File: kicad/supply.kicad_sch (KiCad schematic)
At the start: 52 parts, among them J5 Screw_Terminal_01x02, J6 Screw_Terminal_01x02, U14 TMUX6123, U17 TMUX6123, U19 L7815, U23 L7915, U6 LM2937-5, U9 LM317_TO-252

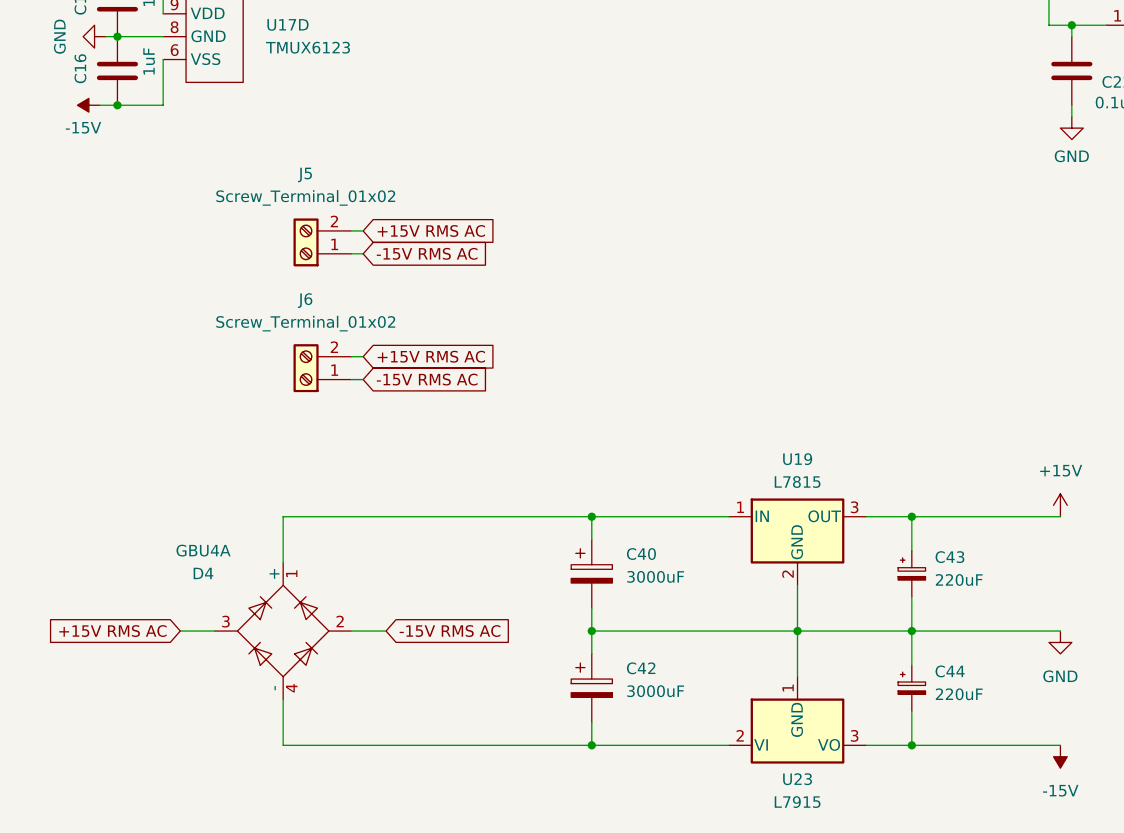
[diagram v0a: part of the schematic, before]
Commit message: Removed large cap and rectifier, added transistor resistors
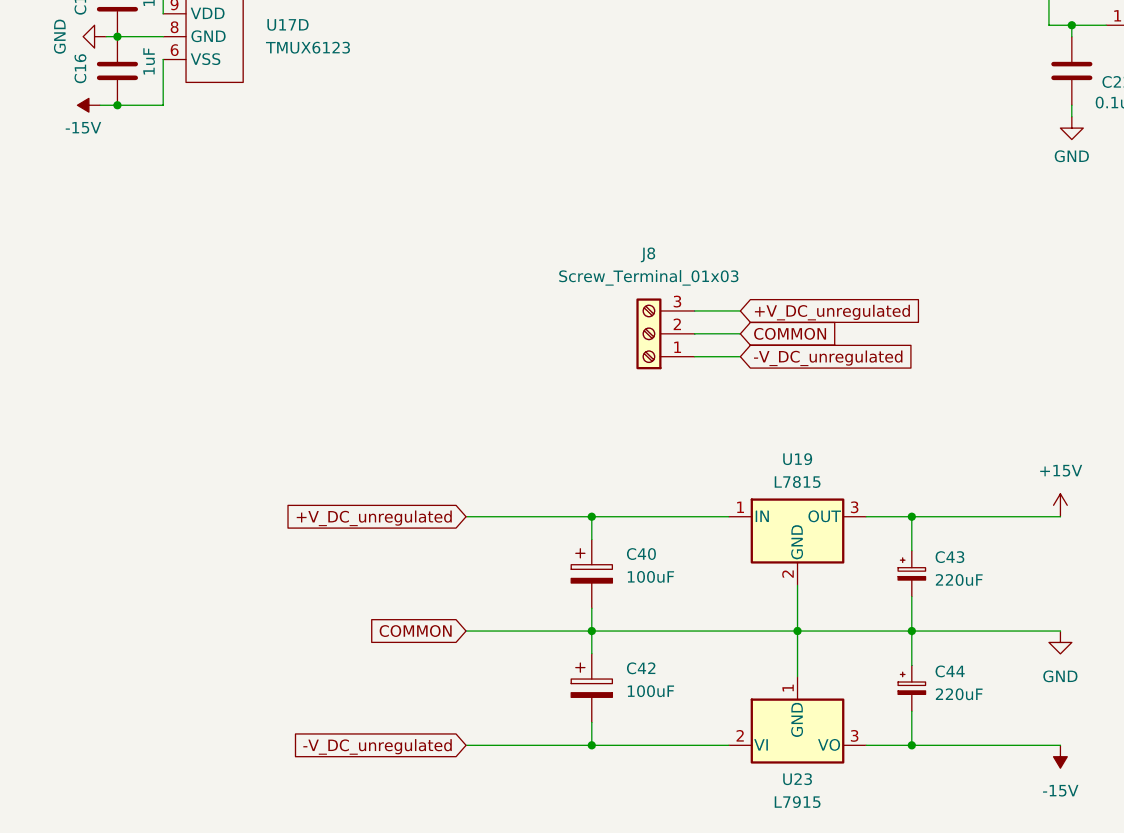
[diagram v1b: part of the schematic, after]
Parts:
- removed D4: GBU4A, Diode_THT:Diode_Bridge_Vishay_GBU, symbol Diode_Bridge:GBU4A
- removed J5, J6: Screw_Terminal_01x02, TerminalBlock_4Ucon:TerminalBlock_4Ucon_1x02_P3.50mm_Horizontal, symbol Connector:Screw_Terminal_01x02
- added J8: Screw_Terminal_01x03, TerminalBlock_4Ucon:TerminalBlock_4Ucon_1x03_P3.50mm_Horizontal, symbol Connector:Screw_Terminal_01x03
- C40, C42: value 3000uF -> 100uF; footprint Capacitor_SMD:CP_Elec_18x22 -> Capacitor_SMD:CP_Elec_8x6.5; DIGIKEY P122523CT-ND -> 1189-35PJV100M6.3X8TR-ND; PARTNO EEE-FK1V302SV -> 35PJV100M6.3X8
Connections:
- net GND: now also J8.2 (Pin_2)
- net +V_DC_unregulated: now reaches C40.1, U19.1 (IN)
- net +V_DC_unregulated: now also J8.3 (Pin_3)
- net -V_DC_unregulated: now reaches C42.2, U23.2 (VI)
- net -V_DC_unregulated: now also J8.1 (Pin_1)

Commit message: Final Schematic, Reworking PCB pt 1
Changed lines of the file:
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@@
 	(wire
 		(pts
-			(xy 72.39 168.91) (xy 86.36 168.91)
-		)
-		(stroke
-			(width 0)
-			(type default)
-		)
-	)
-	(wire
-		(pts
 			(xy 176.53 62.865) (xy 176.53 66.675)
 		)
@@
 	(wire
 		(pts
-			(xy 97.79 135.89) (xy 102.87 135.89)
-		)
-		(stroke
-			(width 0)
-			(type default)
-		)
-	)
-	(wire
-		(pts
 			(xy 160.655 52.07) (xy 176.53 52.07)
 		)
@@
 	(wire
 		(pts
+			(xy 130.81 138.43) (xy 130.81 135.89)
+		)
+		(stroke
+			(width 0)
+			(type default)
+		)
+	)
+	(wire
+		(pts
 			(xy 226.06 112.395) (xy 226.06 113.03)
 		)
@@
 	(wire
 		(pts
+			(xy 130.81 135.89) (xy 97.79 135.89)
+		)
+		(stroke
+			(width 0)
+			(type default)
+		)
+	)
+	(wire
+		(pts
 			(xy 78.74 49.53) (xy 78.74 52.07)
 		)
@@
 		)
 	)
-	(global_label "COMMON"
-		(shape input)
-		(at 72.39 168.91 180)
-		(fields_autoplaced yes)
-		(effects
-			(font
-				(size 1.27 1.27)
-			)
-			(justify right)
-		)
-		(property "Intersheetrefs" "${INTERSHEET_REFS}"
-			(at 61.2405 168.91 0)
-			(effects
-				(font
-					(size 1.27 1.27)
-				)
-				(justify right)
-				(hide yes)
-			)
-		)
-	)
 	(global_label "+V_DC_unregulated"
 		(shape input)
@@
 		)
 	)
-	(global_label "COMMON"
-		(shape input)
-		(at 102.87 135.89 0)
-		(fields_autoplaced yes)
-		(effects
-			(font
-				(size 1.27 1.27)
-			)
-			(justify left)
-		)
-		(property "Intersheetrefs" "${INTERSHEET_REFS}"
-			(at 114.0195 135.89 0)
-			(effects
-				(font
-					(size 1.27 1.27)
-				)
-				(justify left)
-				(hide yes)
-			)
-		)
-	)
 	(global_label "-V_DC_unregulated"
 		(shape input)
@@
 					(unit 1)
 				)
+			)
+		)
+	)
+	(symbol
+		(lib_id "power:GND")
+		(at 130.81 138.43 0)
+		(unit 1)
+		(exclude_from_sim no)
+		(in_bom yes)
+		(on_board yes)
+		(dnp no)
+		(fields_autoplaced yes)
+		(property "Reference" "#PWR081"
+			(at 130.81 144.78 0)
+			(effects
+				(font
+					(size 1.27 1.27)
+				)
+				(hide yes)
+			)
+		)
+		(property "Value" "GND"
+			(at 130.81 143.51 0)
+			(effects
+				(font
+					(size 1.27 1.27)
+				)
+			)
+		)
+		(property "Footprint" ""
+			(at 130.81 138.43 0)
+			(effects
+				(font
+					(size 1.27 1.27)
+				)
+				(hide yes)
+			)
+		)
+		(property "Datasheet" ""
+			(at 130.81 138.43 0)
+			(effects
+				(font
+					(size 1.27 1.27)
+				)
+				(hide yes)
+			)
+		)
+		(property "Description" ""
+			(at 130.81 138.43 0)
+			(effects
+				(font
+					(size 1.27 1.27)
+				)
+				(hide yes)
+			)
+		)
+		(pin "1"
+		)
+		(instances
+			(project "intensity_pi"
+				(path "/3a3d7bcb-6fa5-41ef-9ea1-6d4ab7c492fd/a04c5785-e230-4149-bf27-97ee4701c201"
+					(reference "#PWR081")
+					(unit 1)
+				)

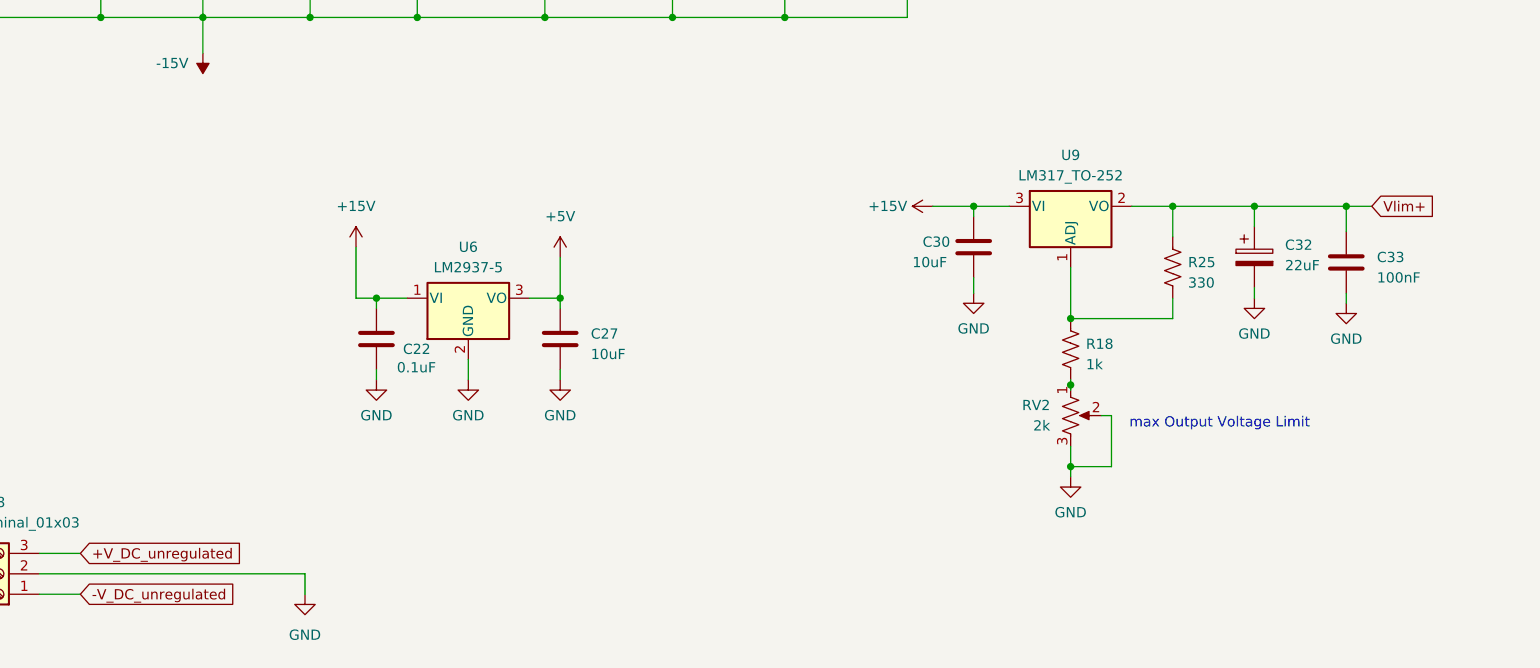
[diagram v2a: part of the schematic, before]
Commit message: Condensed Layout, Removed 5V supply, Shortened Board
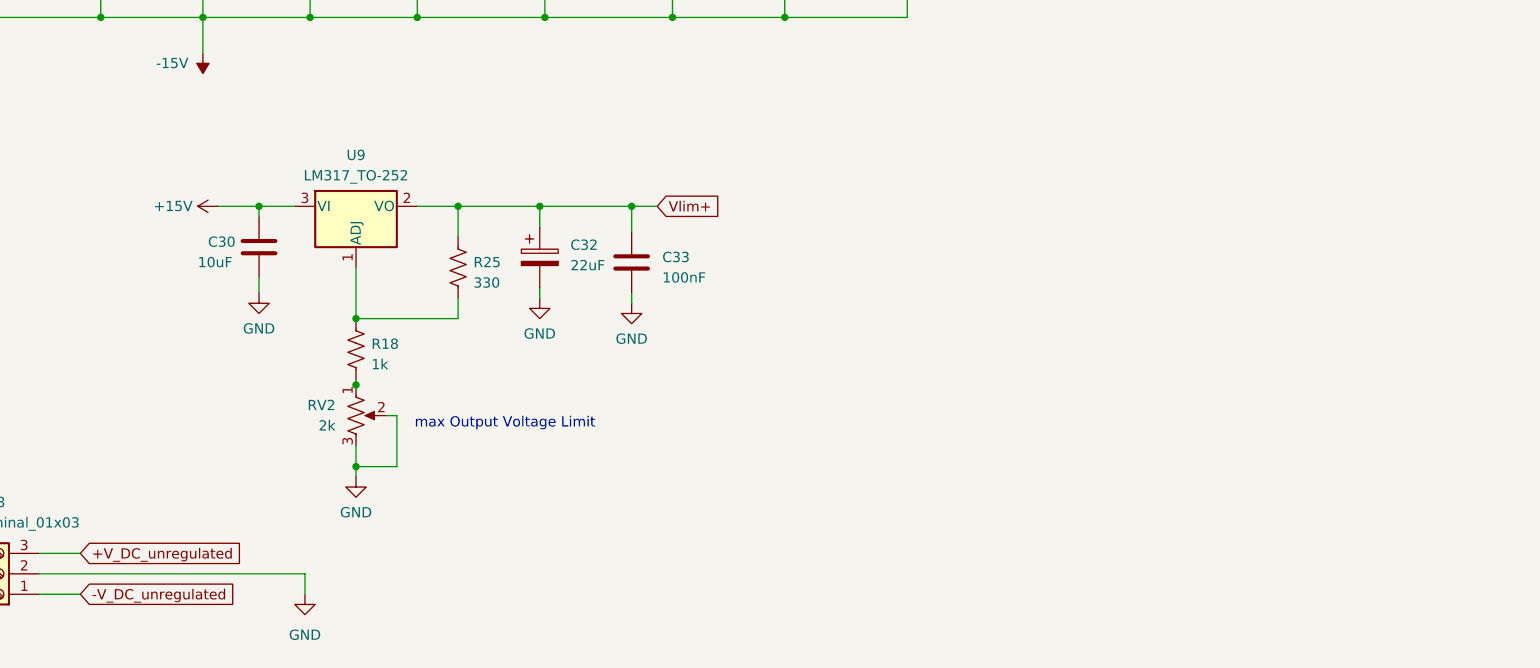
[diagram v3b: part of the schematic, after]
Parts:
- removed C22: 0.1uF, Capacitor_SMD:C_0805_2012Metric, symbol Device:C
- removed C27: 10uF, Capacitor_SMD:C_0805_2012Metric, symbol Device:C
- removed U6: LM2937-5, Package_TO_SOT_SMD:TO-263-3_TabPin2, symbol Regulator_Linear:LM2937xS
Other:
- moved on the sheet: C30, C32, C33, R18, R25, RV2, U9

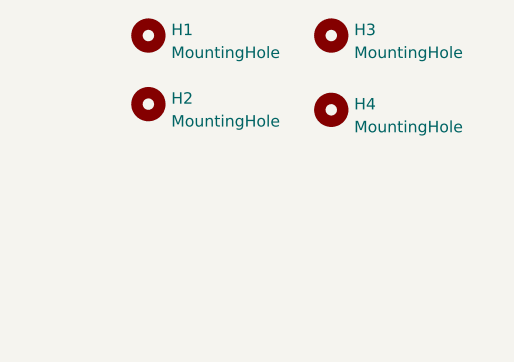
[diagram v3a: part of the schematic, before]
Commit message: Updated Design, more compact layout, precise location values for I/O, Fixed TrimPot footprint, TODO: Finalize BOM, add partnos for SMD R/Cs
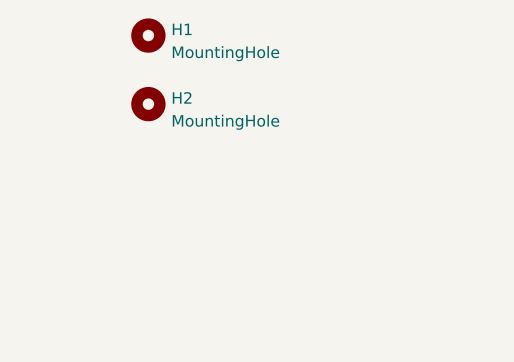
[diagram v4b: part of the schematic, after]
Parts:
- removed H3, H4: MountingHole, MountingHole:MountingHole_3.2mm_M3_ISO14580, symbol Mechanical:MountingHole
- RV2: footprint Connector_PinHeader_2.54mm:PinHeader_1x03_P2.54mm_Vertical -> Potentiometer_THT:Potentiometer_Bourns_3296W_Vertical
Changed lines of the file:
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@@
-	)
-	(symbol
-		(lib_id "Mechanical:MountingHole")
-		(at 264.16 16.51 0)
-		(unit 1)
-		(exclude_from_sim no)
-		(in_bom yes)
-		(on_board yes)
-		(dnp no)
-		(fields_autoplaced yes)
-		(property "Reference" "H3"
-			(at 266.7 15.875 0)
-			(effects
-				(font
-					(size 1.27 1.27)
-				)
-				(justify left)
-			)
-		)
-		(property "Value" "MountingHole"
-			(at 266.7 18.415 0)
-			(effects
-				(font
-					(size 1.27 1.27)
-				)
-				(justify left)
-			)
-		)
-		(property "Footprint" "MountingHole:MountingHole_3.2mm_M3_ISO14580"
-			(at 264.16 16.51 0)
-			(effects
-				(font
-					(size 1.27 1.27)
-				)
-				(hide yes)
-			)
-		)
-		(property "Datasheet" "~"
-			(at 264.16 16.51 0)
-			(effects
-				(font
-					(size 1.27 1.27)
-				)
-				(hide yes)
-			)
-		)
-		(property "Description" ""
-			(at 264.16 16.51 0)
-			(effects
-				(font
-					(size 1.27 1.27)
-				)
-				(hide yes)
-			)
-		)
-		(property "MPN" ""
-			(at 264.16 16.51 0)
-			(effects
-				(font
-					(size 1.27 1.27)
-				)
-				(hide yes)
-			)
-		)
-		(instances
-			(project "progress_intensity_pi"
-				(path "/3a3d7bcb-6fa5-41ef-9ea1-6d4ab7c492fd/a04c5785-e230-4149-bf27-97ee4701c201"
-					(reference "H3")
-					(unit 1)
-				)
-			)
-		)
 	)
 	(symbol
@@
 	)
 	(symbol
-		(lib_id "Mechanical:MountingHole")
-		(at 264.16 24.765 0)
-		(unit 1)
-		(exclude_from_sim no)
-		(in_bom yes)
-		(on_board yes)
-		(dnp no)
-		(fields_autoplaced yes)
-		(property "Reference" "H4"
-			(at 266.7 24.13 0)
-			(effects
-				(font
-					(size 1.27 1.27)
-				)
-				(justify left)
-			)
-		)
-		(property "Value" "MountingHole"
-			(at 266.7 26.67 0)
-			(effects
-				(font
-					(size 1.27 1.27)
-				)
-				(justify left)
-			)
-		)
-		(property "Footprint" "MountingHole:MountingHole_3.2mm_M3_ISO14580"
-			(at 264.16 24.765 0)
-			(effects
-				(font
-					(size 1.27 1.27)
-				)
-				(hide yes)
-			)
-		)
-		(property "Datasheet" "~"
-			(at 264.16 24.765 0)
-			(effects
-				(font
-					(size 1.27 1.27)
-				)
-				(hide yes)
-			)
-		)
-		(property "Description" ""
-			(at 264.16 24.765 0)
-			(effects
-				(font
-					(size 1.27 1.27)
-				)
-				(hide yes)
-			)
-		)
-		(property "MPN" ""
-			(at 264.16 24.765 0)
-			(effects
-				(font
-					(size 1.27 1.27)
-				)
-				(hide yes)
-			)
-		)
-		(instances
-			(project "progress_intensity_pi"
-				(path "/3a3d7bcb-6fa5-41ef-9ea1-6d4ab7c492fd/a04c5785-e230-4149-bf27-97ee4701c201"
-					(reference "H4")
-					(unit 1)
-				)
-			)
-		)
-	)
-	(symbol
 		(lib_id "Device:R_US")
 		(at 137.16 107.95 180)
@@
 			)
 		)
-		(property "Footprint" "Connector_PinHeader_2.54mm:PinHeader_1x03_P2.54mm_Vertical"
+		(property "Footprint" "Potentiometer_THT:Potentiometer_Bourns_3296W_Vertical"
 			(at 137.16 116.205 0)
 			(effects

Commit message: Minor Layout updates, replaced old component part no's, added part no's for rest of parts
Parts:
- C13, C16, C2, C3: DIGIKEY (none) -> 1276-6469-2-ND; PARTNO (none) -> CL21B105KAFNNNG
- C14, C15, C17, C18, C19, C20, C21, C23, C24, C26, C28, C29, C31, C33, C36, C37, C38, C39, C4, C5, C6, C7, C8, C9: DIGIKEY (none) -> 1276-6840-2-ND; PARTNO (none) -> CL21B104KCFNNNE
- C30: DIGIKEY (none) -> 1276-3387-2-ND; PARTNO (none) -> CL32B106KBJNNNE
- J8: DIGIKEY (none) -> 732-2748-ND; PARTNO (none) -> 691214110003
- R18: DIGIKEY (none) -> 5831-2-2176327-5TR-ND; PARTNO (none) -> 2-2176327-5
- R25: DIGIKEY (none) -> RMCF0805FT330RTR-ND; PARTNO (none) -> RMCF0805FT330R

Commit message: Fixed Digikey Part numbers for some parts, confirmed final BOM, Fixed Switch Footprint hole size
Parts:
- C13, C16, C2, C3: DIGIKEY 1276-6469-2-ND -> 1276-6469-1-ND
- C14, C15, C17, C18, C19, C20, C21, C23, C24, C26, C28, C29, C31, C33, C36, C37, C38, C39, C4, C5, C6, C7, C8, C9: DIGIKEY 1276-6840-2-ND -> 1276-6840-1-ND
- C30: DIGIKEY 1276-3387-2-ND -> 1276-3387-1-ND
- C40, C42: DIGIKEY 1189-35PJV100M6.3X8TR-ND -> 1189-35PJV100M6.3X8CT-ND
- R18: DIGIKEY 5831-2-2176327-5TR-ND -> RG20P1.0KBCT-ND; PARTNO 2-2176327-5 -> RG2012P-102-B-T5
- R25: DIGIKEY RMCF0805FT330RTR-ND -> RMCF0805FT330RCT-ND
- U19: DIGIKEY MC7815BDTRKG -> MC7815BDTRKGOSCT-ND
- U23: DIGIKEY MC7915ACD2TG -> MC7915ACD2TGOS-ND
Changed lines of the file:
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@@
 			)
 		)
-		(property "DIGIKEY" "1276-6840-2-ND "
+		(property "DIGIKEY" "1276-6840-1-ND "
 			(at 190.5 45.72 0)
 			(effects
@@
 			)
 		)
-		(property "DIGIKEY" "1276-6840-2-ND "
+		(property "DIGIKEY" "1276-6840-1-ND "
 			(at 78.74 59.055 0)
 			(effects
@@
 			)
 		)
-		(property "DIGIKEY" "1276-6840-2-ND "
+		(property "DIGIKEY" "1276-6840-1-ND "
 			(at 105.41 59.055 0)
 			(effects
@@
 			)
 		)
-		(property "DIGIKEY" "1276-6840-2-ND "
+		(property "DIGIKEY" "1276-6840-1-ND "
 			(at 78.74 45.72 0)
 			(effects
@@
 			)
 		)
-		(property "DIGIKEY" "1276-6840-2-ND "
+		(property "DIGIKEY" "1276-6840-1-ND "
 			(at 118.11 59.055 0)
 			(effects
@@
 			)
 		)
-		(property "DIGIKEY" "1276-6469-2-ND"
+		(property "DIGIKEY" "1276-6469-1-ND"
 			(at 33.02 83.82 90)
 			(effects
@@
 			)
 		)
-		(property "DIGIKEY" "1276-6840-2-ND "
+		(property "DIGIKEY" "1276-6840-1-ND "
 			(at 160.655 45.72 0)
 			(effects
@@
 			)
 		)
-		(property "DIGIKEY" "1276-6840-2-ND "
+		(property "DIGIKEY" "1276-6840-1-ND "
 			(at 52.07 59.055 0)
 			(effects
@@
 			)
 		)
-		(property "DIGIKEY" "1276-6840-2-ND "
+		(property "DIGIKEY" "1276-6840-1-ND "
 			(at 160.655 59.055 0)
 			(effects
@@
 			)
 		)
-		(property "DIGIKEY" "1276-6840-2-ND "
+		(property "DIGIKEY" "1276-6840-1-ND "
 			(at 205.74 45.72 0)
 			(effects
@@
 			)
 		)
-		(property "DIGIKEY" "1276-6840-2-ND "
+		(property "DIGIKEY" "1276-6840-1-ND "
 			(at 52.07 45.72 0)
 			(effects
@@
 			)
 		)
-		(property "DIGIKEY" "1276-6469-2-ND"
+		(property "DIGIKEY" "1276-6469-1-ND"
 			(at 33.02 76.2 90)
 			(effects
@@
 			)
 		)
-		(property "DIGIKEY" "1276-6840-2-ND "
+		(property "DIGIKEY" "1276-6840-1-ND "
 			(at 92.075 59.055 0)
 			(effects
@@
 			)
 		)
-		(property "DIGIKEY" "1276-6840-2-ND "
+		(property "DIGIKEY" "1276-6840-1-ND "
 			(at 65.405 45.72 0)
 			(effects
@@
 			)
 		)
-		(property "DIGIKEY" "5831-2-2176327-5TR-ND"
+		(property "DIGIKEY" "RG20P1.0KBCT-ND"
 			(at 137.16 107.95 0)
 			(effects
@@
 			)
 		)
-		(property "PARTNO" "2-2176327-5"
+		(property "PARTNO" "RG2012P-102-B-T5"
 			(at 137.16 107.95 0)
 			(effects
@@
 			)
 		)
-		(property "DIGIKEY" "1276-6840-2-ND "
+		(property "DIGIKEY" "1276-6840-1-ND "
 			(at 205.74 59.055 0)
 			(effects
@@
 			)
 		)
-		(property "DIGIKEY" "1276-6840-2-ND "
+		(property "DIGIKEY" "1276-6840-1-ND "
 			(at 65.405 59.055 0)
 			(effects
@@
 			)
 		)
-		(property "DIGIKEY" "1276-6840-2-ND "
+		(property "DIGIKEY" "1276-6840-1-ND "
 			(at 118.11 45.72 0)
 			(effects
@@
 			)
 		)
-		(property "DIGIKEY" "1276-6840-2-ND "
+		(property "DIGIKEY" "1276-6840-1-ND "
 			(at 176.53 45.72 0)
 			(effects
@@
 			)
 		)
-		(property "DIGIKEY" "1276-6840-2-ND "
+		(property "DIGIKEY" "1276-6840-1-ND "
 			(at 131.445 45.72 0)
 			(effects
@@
 			)
 		)
-		(property "DIGIKEY" "RMCF0805FT330RTR-ND"
+		(property "DIGIKEY" "RMCF0805FT330RCT-ND"
 			(at 149.86 97.79 0)
 			(effects
@@
 			)
 		)
-		(property "DIGIKEY" "1276-6840-2-ND "
+		(property "DIGIKEY" "1276-6840-1-ND "
 			(at 176.53 59.055 0)
 			(effects
@@
 			)
 		)
-		(property "DIGIKEY" "1276-3387-2-ND"
+		(property "DIGIKEY" "1276-3387-1-ND"
 			(at 125.095 95.25 0)
 			(effects
@@
 			)
 		)
-		(property "DIGIKEY" "MC7815BDTRKG"
+		(property "DIGIKEY" "MC7815BDTRKGOSCT-ND"
 			(at 109.22 156.21 0)
 			(effects
@@
 			)
 		)
-		(property "DIGIKEY" "1276-6840-2-ND "
+		(property "DIGIKEY" "1276-6840-1-ND "
 			(at 144.78 59.055 0)
 			(effects
@@
 			)
 		)
-		(property "DIGIKEY" "1276-6469-2-ND"
+		(property "DIGIKEY" "1276-6469-1-ND"
 			(at 33.655 99.06 90)
 			(effects
@@
 			)
 		)
-		(property "DIGIKEY" "1276-6469-2-ND"
+		(property "DIGIKEY" "1276-6469-1-ND"
 			(at 33.655 106.68 90)
 			(effects
@@
 			)
 		)
-		(property "DIGIKEY" "1276-6840-2-ND "
+		(property "DIGIKEY" "1276-6840-1-ND "
 			(at 92.075 45.72 0)
 			(effects
@@
 			)
 		)
-		(property "DIGIKEY" "1276-6840-2-ND "
+		(property "DIGIKEY" "1276-6840-1-ND "
 			(at 190.5 59.055 0)
 			(effects
@@
 			)
 		)
-		(property "DIGIKEY" "MC7915ACD2TG"
+		(property "DIGIKEY" "MC7915ACD2TGOS-ND"
 			(at 109.22 181.61 0)
 			(effects
@@
 			)
 		)
-		(property "DIGIKEY" "1276-6840-2-ND "
+		(property "DIGIKEY" "1276-6840-1-ND "
 			(at 131.445 59.055 0)
 			(effects
@@
 			)
 		)
-		(property "DIGIKEY" "1276-6840-2-ND "
+		(property "DIGIKEY" "1276-6840-1-ND "
 			(at 171.45 97.155 0)
 			(effects
@@
 			)
 		)
-		(property "DIGIKEY" "1189-35PJV100M6.3X8TR-ND"
+		(property "DIGIKEY" "1189-35PJV100M6.3X8CT-ND"
 			(at 86.36 162.56 0)
 			(effects
@@
 			)
 		)
-		(property "DIGIKEY" "1189-35PJV100M6.3X8TR-ND"
+		(property "DIGIKEY" "1189-35PJV100M6.3X8CT-ND"
 			(at 86.36 175.26 0)
 			(effects
@@
 			)
 		)
-		(property "DIGIKEY" "1276-6840-2-ND "
+		(property "DIGIKEY" "1276-6840-1-ND "
 			(at 144.78 45.72 0)
 			(effects

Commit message: V1.1, Fixedincorrect footprints for Green/Red LED, Diodes, Mosfets, Flipped Input A/B Polarity, Potentiometer labels, Incorrect part nos for V regulators. No functionality changes
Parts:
- U19, U23: footprint Package_TO_SOT_SMD:TO-252-3_TabPin2 -> Package_TO_SOT_SMD:TO-263-3_TabPin2
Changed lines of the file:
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@@
 			)
 		)
-		(property "Footprint" "Package_TO_SOT_SMD:TO-252-3_TabPin2"
+		(property "Footprint" "Package_TO_SOT_SMD:TO-263-3_TabPin2"
 			(at 109.855 160.02 0)
 			(effects
@@
 			)
 		)
-		(property "Footprint" "Package_TO_SOT_SMD:TO-252-3_TabPin2"
+		(property "Footprint" "Package_TO_SOT_SMD:TO-263-3_TabPin2"
 			(at 109.22 186.69 0)
 			(effects
